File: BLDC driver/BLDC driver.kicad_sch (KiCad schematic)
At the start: 41 parts, among them J1 Screw_Terminal_01x02, J2 Screw_Terminal_01x03, J3 Conn_02x06_Counter_Clockwise, J4 Izlaz ocitavanje struje, Q1 N0436N, Q2 N0436N, Q3 N0436N, Q4 N0436N, Q5 N0436N, Q6 N0436N, U1 MCP8027T-H/Y4X

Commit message: Ispravljene greske
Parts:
- R18, R4, R5, R6, R7, R8: value R_US -> 20
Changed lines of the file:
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@@
 			)
 		)
-		(property "Value" "R_US"
+		(property "Value" "20"
 			(at 158.242 86.868 90)
 			(effects
@@
 			)
 		)
-		(property "Value" "R_US"
+		(property "Value" "20"
 			(at 182.372 114.808 90)
 			(effects
@@
 			)
 		)
-		(property "Value" "R_US"
+		(property "Value" "20"
 			(at 158.242 108.458 90)
 			(effects
@@
 			)
 		)
-		(property "Value" "R_US"
+		(property "Value" "20"
 			(at 181.102 89.408 90)
 			(effects
@@
 			)
 		)
-		(property "Value" "R_US"
+		(property "Value" "20"
 			(at 209.042 121.158 90)
 			(effects
@@
 			)
 		)
-		(property "Value" "R_US"
+		(property "Value" "20"
 			(at 207.772 95.758 90)
 			(effects

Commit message: Novi shunt-ovi
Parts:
- R1, R2, R3: value 0.01 -> WSLP2512R0100FEA; footprint Resistor_SMD:R_Shunt_Vishay_WSR2_WSR3_KelvinConnection -> Resistor_SMD:R_2512_6332Metric_Pad1.40x3.35mm_HandSolder
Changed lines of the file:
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@@
 			)
 		)
-		(property "Value" "0.01"
+		(property "Value" "WSLP2512R0100FEA"
 			(at 219.71 149.8599 0)
 			(effects
@@
 			)
 		)
-		(property "Footprint" "Resistor_SMD:R_Shunt_Vishay_WSR2_WSR3_KelvinConnection"
+		(property "Footprint" "Resistor_SMD:R_2512_6332Metric_Pad1.40x3.35mm_HandSolder"
 			(at 218.186 148.844 90)
 			(effects
@@
 			)
 		)
-		(property "Value" "0.01"
+		(property "Value" "WSLP2512R0100FEA"
 			(at 194.31 138.4299 0)
 			(effects
@@
 			)
 		)
-		(property "Footprint" "Resistor_SMD:R_Shunt_Vishay_WSR2_WSR3_KelvinConnection"
+		(property "Footprint" "Resistor_SMD:R_2512_6332Metric_Pad1.40x3.35mm_HandSolder"
 			(at 192.786 137.414 90)
 			(effects
@@
 			)
 		)
-		(property "Value" "0.01"
+		(property "Value" "WSLP2512R0100FEA"
 			(at 170.18 126.9999 0)
 			(effects
@@
 			)
 		)
-		(property "Footprint" "Resistor_SMD:R_Shunt_Vishay_WSR2_WSR3_KelvinConnection"
+		(property "Footprint" "Resistor_SMD:R_2512_6332Metric_Pad1.40x3.35mm_HandSolder"
 			(at 168.656 125.984 90)
 			(effects

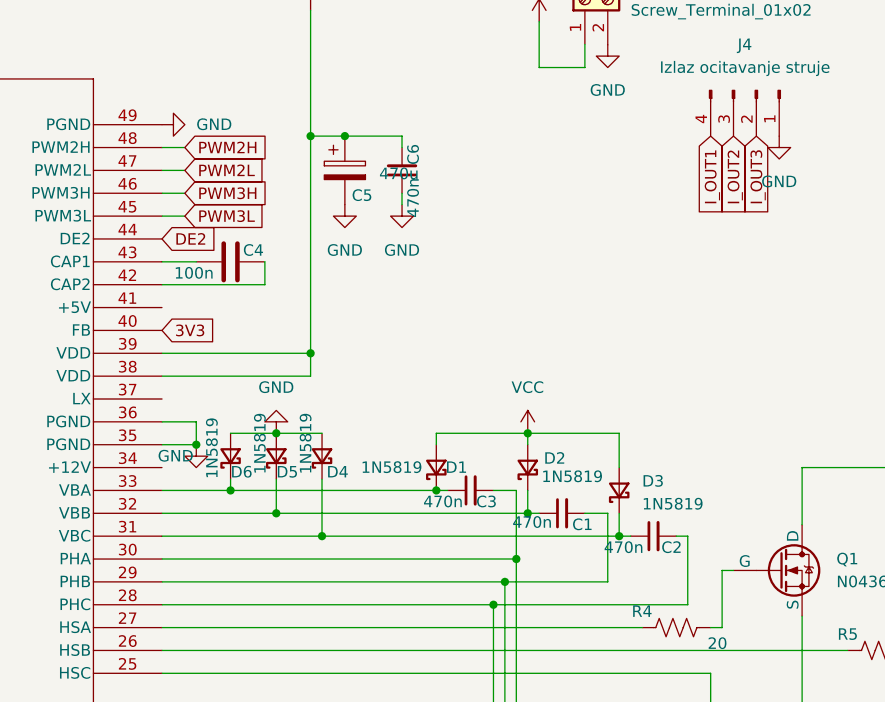
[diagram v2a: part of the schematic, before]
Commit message: Promenjene diode usled greske
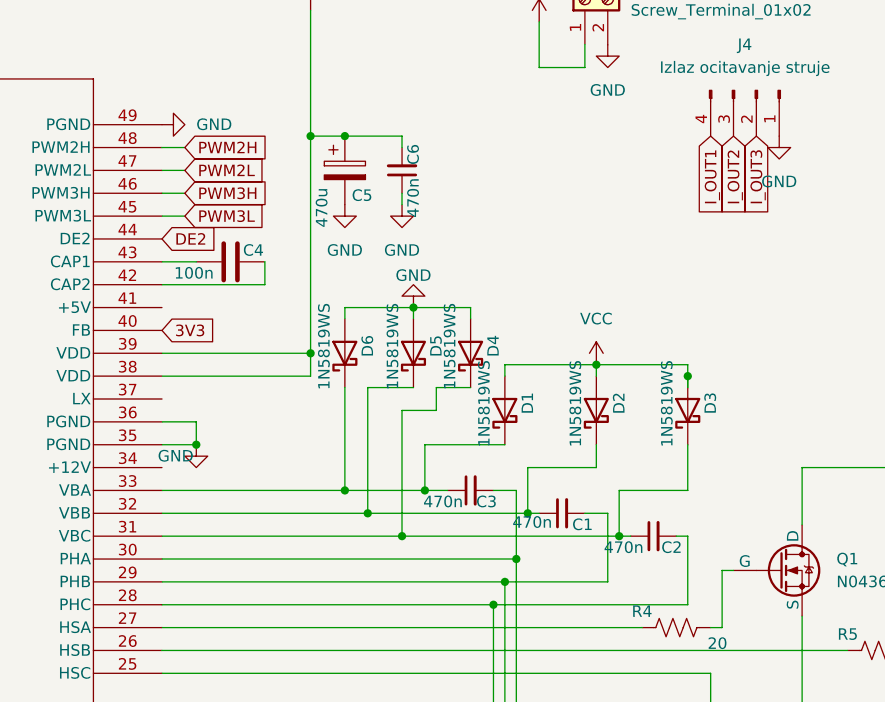
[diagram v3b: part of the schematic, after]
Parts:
- removed D1, D2, D3, D4, D5, D6: 1N5819, Diode_SMD:D_0603_1608Metric_Pad1.05x0.95mm_HandSolder, symbol Device:D_Schottky_Small
- added D1, D2, D3, D4, D5, D6: 1N5819WS, Diode_SMD:D_SOD-323_HandSoldering, symbol Diode:1N5819WS
- C5: footprint Capacitor_THT:CP_Radial_D10.0mm_P7.50mm -> Capacitor_THT:CP_Radial_D10.0mm_P5.00mm
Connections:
- net GND: now also D4.2 (A), D5.2 (A), D6.2 (A)
- net VCC: now also D1.2 (A), D2.2 (A), D3.2 (A)
- net at C2.1, U1.31 (VBC): now also D3.1 (K), D4.1 (K)
- net at C3.1, U1.33 (VBA): now also D1.1 (K), D6.1 (K)
- net at C1.1, U1.32 (VBB): now also D2.1 (K), D5.1 (K)

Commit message: Dodadi kondenzatori, vratiti u slucaju greske
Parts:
- added C10, C11, C12, C13, C14, C15, C16, C17, C18, C19, C20, C21, C22, C23, C24, C7, C8, C9: 470n, Capacitor_SMD:C_0603_1608Metric_Pad1.08x0.95mm_HandSolder, symbol Device:C_Small
- added H1, H2, H3, H4: MountingHole, MountingHole:MountingHole_3.2mm_M3, symbol Mechanical:MountingHole
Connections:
- net GND: now also Q4.3 (S), Q5.3 (S), Q6.3 (S), R1.1, R11.1, R11.2, R12.2, R2.1, R3.1, R8.1, R9.2, U1.11 (ISENSE3+), U1.22 (LSB), C10.2, C11.2, C12.2, C13.2, C14.2, C15.2, C16.2, C17.2, C18.2, C19.2, C20.2, C21.2, C22.2, C23.2, C24.2, C7.2, C8.2, C9.2
- net VCC: now also C10.1, C11.1, C12.1, C13.1, C14.1, C15.1, C16.1, C17.1, C18.1, C19.1, C20.1, C21.1, C22.1, C23.1, C24.1, C7.1, C8.1, C9.1
- net at C3.2, J2.1 (Pin_1), Q1.3 (S)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: now also C2.2, J2.3 (Pin_3), Q3.3 (S), Q6.1 (D), U1.28 (PHC)
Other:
- moved on the sheet: C1, C2, C3, D1, D2, D3, D4, D5, D6, J2, Q1, Q2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

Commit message: Dodati test point-ovi
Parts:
- added TP1, TP2, TP3, TP4, TP5, TP6, TP7: TestPoint, TestPoint:TestPoint_Pad_D3.0mm, symbol Connector:TestPoint
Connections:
- net GND: no longer Q4.3 (S), Q5.3 (S), Q6.3 (S), R1.1, R11.1, R11.2, R12.2, R2.1, R3.1, R8.1, R9.2, U1.11 (ISENSE3+), U1.22 (LSB)
- net at R18.1: now also U1.22 (LSB); no longer U1.23 (LSC)
- net at U1.34 (+12V): now also TP1.1
- net at U1.37 (LX): now also TP2.1
- net at U1.4 (LV_OUT2): now also TP4.1
- net at U1.41 (+5V): now also TP3.1
- net at U1.5 (HV_IN2): now also TP5.1
- net at U1.6 (HV_IN1): now also TP6.1
- net at U1.8 (LV_OUT1): now also TP7.1
- new net: Q6.3 (S), R12.2, R3.1
- new net: R11.1, U1.11 (ISENSE3+)
- new net: R8.1, U1.23 (LSC)
- new net: Q5.3 (S), R2.1, R9.2
- new net: Q4.3 (S), R1.1, R11.2
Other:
- moved on the sheet: R10, R11, R12, R13, R14, R9

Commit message: Dodati test pointovi, novi screw konektori i BOM
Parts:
- J1: footprint TerminalBlock:TerminalBlock_Altech_AK300-2_P5.00mm -> TerminalBlock_Phoenix:TerminalBlock_Phoenix_MKDS-1,5-2-5.08_1x02_P5.08mm_Horizontal
- J2: footprint TerminalBlock:TerminalBlock_Altech_AK300-3_P5.00mm -> TerminalBlock_Phoenix:TerminalBlock_Phoenix_MKDS-1,5-3-5.08_1x03_P5.08mm_Horizontal
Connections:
- net at C3.2, J2.1 (Pin_1), Q1.3 (S)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: no longer C2.2, J2.3 (Pin_3), Q3.3 (S), Q6.1 (D), U1.28 (PHC)
- net at U1.22 (LSB): now also R8.1; no longer R18.1
- net at U1.23 (LSC): now also R18.1; no longer R8.1
- new net: C2.2, J2.3 (Pin_3), Q3.3 (S), Q6.1 (D), U1.28 (PHC)
